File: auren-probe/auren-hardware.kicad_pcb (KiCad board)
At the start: 2 copper layers, 24.4 x 22.2 mm, 12 parts, among them J1 HDMI_Micro-D_Molex_46765-1x01, J3 Speaker_1, J4 Speaker_2

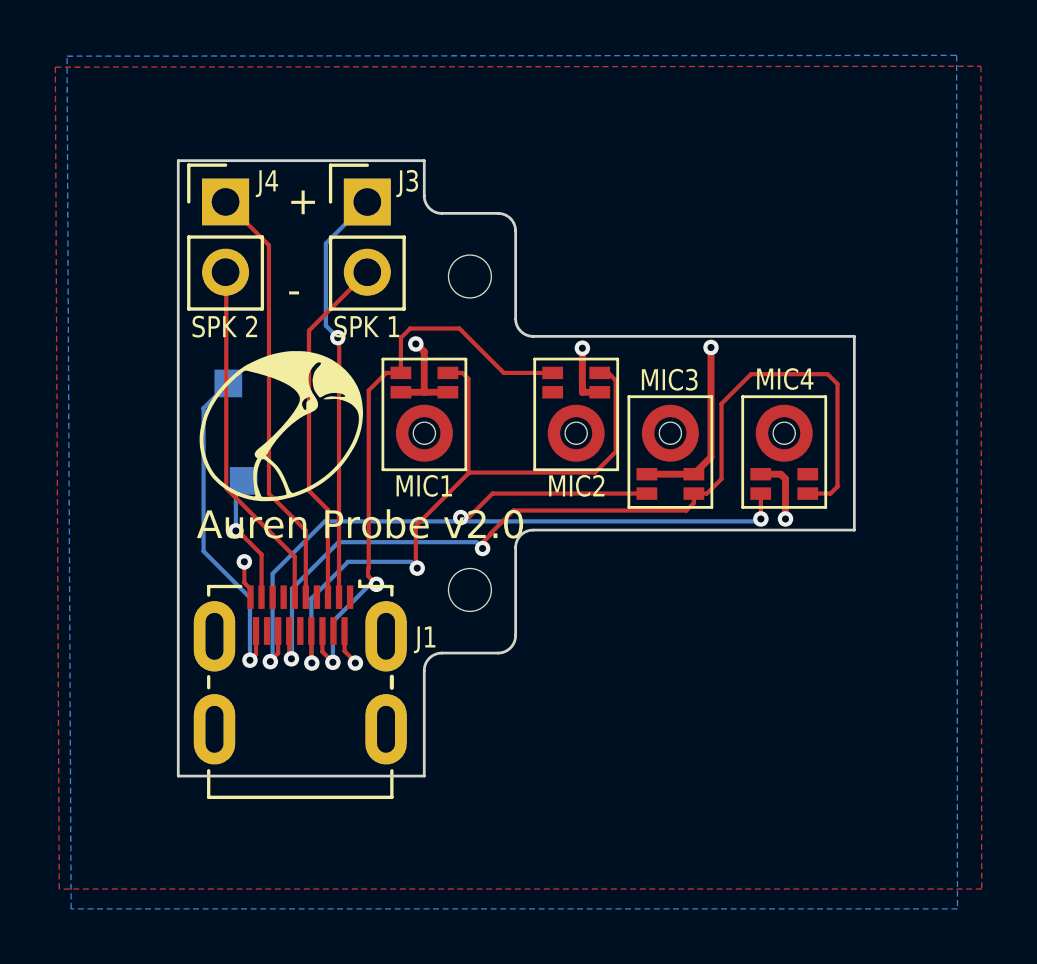
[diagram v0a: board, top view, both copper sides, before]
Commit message: added top bottom png files
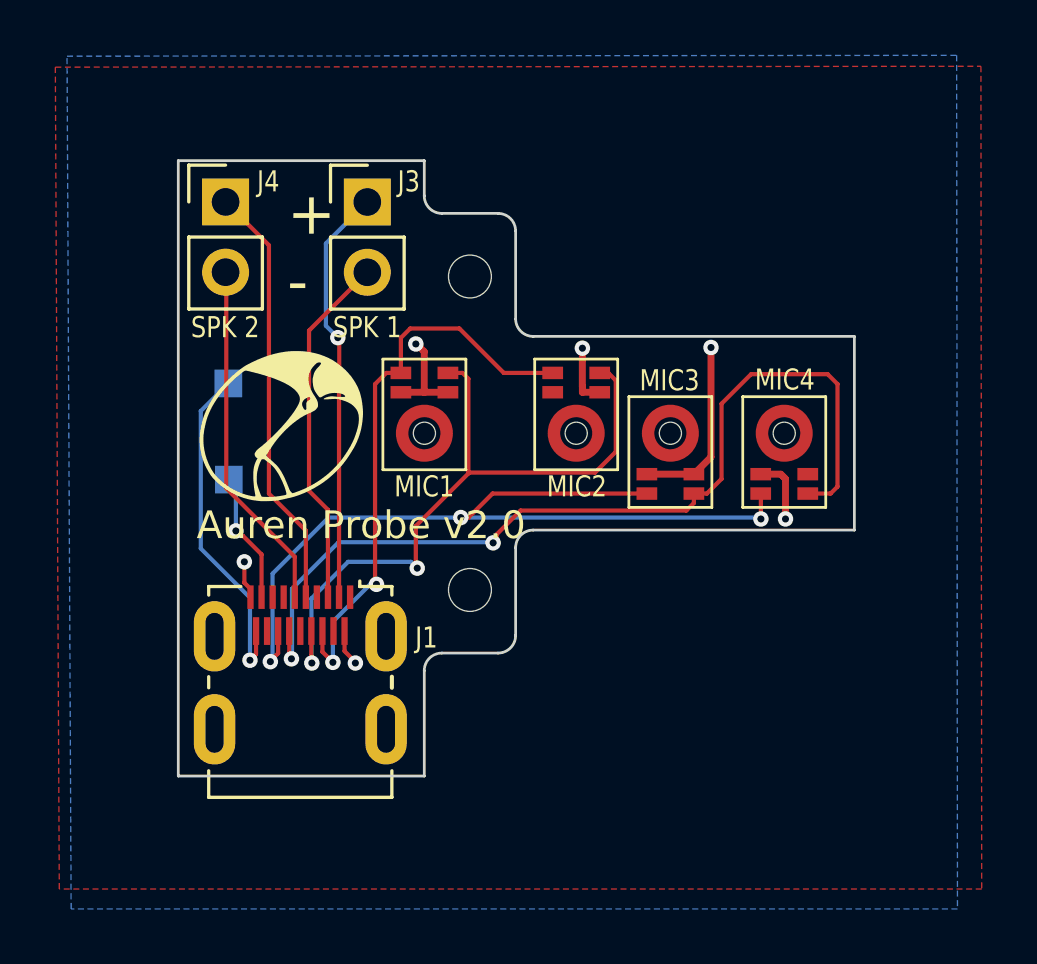
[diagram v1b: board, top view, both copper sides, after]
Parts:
- moved TP1 0.54 mm to (140.2, 106.8)
